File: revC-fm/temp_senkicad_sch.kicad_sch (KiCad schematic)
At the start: 4 parts, among them U32 MCP9700AT-E/LT

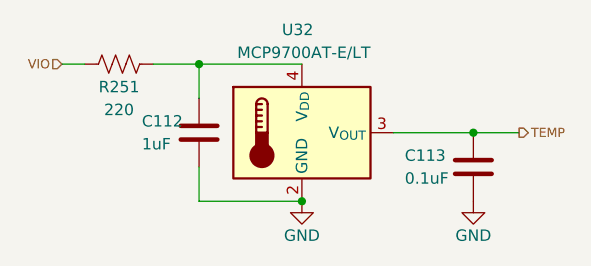
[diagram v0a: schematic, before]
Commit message: updated per review, improved docs
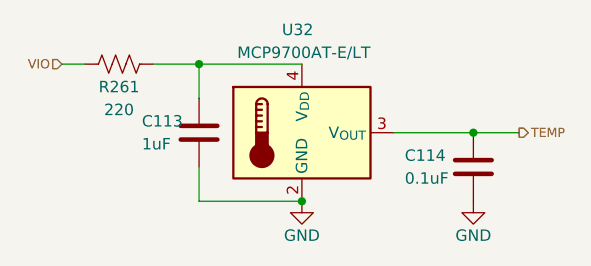
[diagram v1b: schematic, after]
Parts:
- renumbered C112 to C113, C113 to C114, R251 to R261
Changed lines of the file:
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@@
   (symbol (lib_id "power:GND") (at 148.59 104.14 0) (unit 1)
     (in_bom yes) (on_board yes) (dnp no)
-    (property "Reference" "#PWR0175" (at 148.59 110.49 0)
+    (property "Reference" "#PWR0180" (at 148.59 110.49 0)
       (effects (font (size 1.27 1.27)) hide)
     )
@@
       (project "mainboard"
         (path "/d1441985-7b63-4bf8-a06d-c70da2e3b78b/cda1ad7d-3729-4e28-9f04-75ded2a9befd/8821f222-8792-4e4d-9d02-2f4e81ef493f"
-          (reference "#PWR0175") (unit 1)
-        )
-        (path "/d1441985-7b63-4bf8-a06d-c70da2e3b78b/cda1ad7d-3729-4e28-9f04-75ded2a9befd/795619f3-8bd8-4f29-a923-296e7ed8459e"
-          (reference "#PWR0177") (unit 1)
-        )
-        (path "/d1441985-7b63-4bf8-a06d-c70da2e3b78b/cda1ad7d-3729-4e28-9f04-75ded2a9befd/e299339d-e625-4f2c-804c-bf3cf31a6799"
-          (reference "#PWR0179") (unit 1)
-        )
-        (path "/d1441985-7b63-4bf8-a06d-c70da2e3b78b/cda1ad7d-3729-4e28-9f04-75ded2a9befd/ea7f9fd6-aeb6-4ec9-906e-e84511ddb647"
-          (reference "#PWR0181") (unit 1)
+          (reference "#PWR0180") (unit 1)
+        )
+        (path "/d1441985-7b63-4bf8-a06d-c70da2e3b78b/cda1ad7d-3729-4e28-9f04-75ded2a9befd/795619f3-8bd8-4f29-a923-296e7ed8459e"
+          (reference "#PWR0182") (unit 1)
+        )
+        (path "/d1441985-7b63-4bf8-a06d-c70da2e3b78b/cda1ad7d-3729-4e28-9f04-75ded2a9befd/e299339d-e625-4f2c-804c-bf3cf31a6799"
+          (reference "#PWR0184") (unit 1)
+        )
+        (path "/d1441985-7b63-4bf8-a06d-c70da2e3b78b/cda1ad7d-3729-4e28-9f04-75ded2a9befd/ea7f9fd6-aeb6-4ec9-906e-e84511ddb647"
+          (reference "#PWR0186") (unit 1)
         )
       )
@@
   (symbol (lib_id "Device:R_US") (at 109.22 88.9 90) (unit 1)
     (in_bom yes) (on_board yes) (dnp no)
-    (property "Reference" "R251" (at 109.22 91.44 90)
+    (property "Reference" "R261" (at 109.22 91.44 90)
       (effects (font (size 1.27 1.27)))
     )
@@
       (effects (font (size 1.27 1.27)) hide)
     )
-    (pin "1")
-    (pin "2")
-    (instances
-      (project "mainboard"
-        (path "/d1441985-7b63-4bf8-a06d-c70da2e3b78b/cda1ad7d-3729-4e28-9f04-75ded2a9befd/8821f222-8792-4e4d-9d02-2f4e81ef493f"
-          (reference "R251") (unit 1)
-        )
-        (path "/d1441985-7b63-4bf8-a06d-c70da2e3b78b/cda1ad7d-3729-4e28-9f04-75ded2a9befd/795619f3-8bd8-4f29-a923-296e7ed8459e"
-          (reference "R252") (unit 1)
-        )
-        (path "/d1441985-7b63-4bf8-a06d-c70da2e3b78b/cda1ad7d-3729-4e28-9f04-75ded2a9befd/e299339d-e625-4f2c-804c-bf3cf31a6799"
-          (reference "R253") (unit 1)
-        )
-        (path "/d1441985-7b63-4bf8-a06d-c70da2e3b78b/cda1ad7d-3729-4e28-9f04-75ded2a9befd/ea7f9fd6-aeb6-4ec9-906e-e84511ddb647"
-          (reference "R254") (unit 1)
+    (property "Description" "RES 220 OHM 1% 1/10W 0603" (at 109.22 88.9 0)
+      (effects (font (size 1.27 1.27)) hide)
+    )
+    (pin "1")
+    (pin "2")
+    (instances
+      (project "mainboard"
+        (path "/d1441985-7b63-4bf8-a06d-c70da2e3b78b/cda1ad7d-3729-4e28-9f04-75ded2a9befd/8821f222-8792-4e4d-9d02-2f4e81ef493f"
+          (reference "R261") (unit 1)
+        )
+        (path "/d1441985-7b63-4bf8-a06d-c70da2e3b78b/cda1ad7d-3729-4e28-9f04-75ded2a9befd/795619f3-8bd8-4f29-a923-296e7ed8459e"
+          (reference "R262") (unit 1)
+        )
+        (path "/d1441985-7b63-4bf8-a06d-c70da2e3b78b/cda1ad7d-3729-4e28-9f04-75ded2a9befd/e299339d-e625-4f2c-804c-bf3cf31a6799"
+          (reference "R263") (unit 1)
+        )
+        (path "/d1441985-7b63-4bf8-a06d-c70da2e3b78b/cda1ad7d-3729-4e28-9f04-75ded2a9befd/ea7f9fd6-aeb6-4ec9-906e-e84511ddb647"
+          (reference "R264") (unit 1)
         )
       )
@@
     )
     (property "Manufacturer" "Microchip Technology" (at 129.54 96.52 0)
+      (effects (font (size 1.27 1.27)) hide)
+    )
+    (property "Description" "SENSOR ANALOG -40C-125C SC70-5" (at 129.54 96.52 0)
       (effects (font (size 1.27 1.27)) hide)
     )
@@
   (symbol (lib_id "power:GND") (at 129.54 104.14 0) (unit 1)
     (in_bom yes) (on_board yes) (dnp no)
-    (property "Reference" "#PWR0174" (at 129.54 110.49 0)
+    (property "Reference" "#PWR0179" (at 129.54 110.49 0)
       (effects (font (size 1.27 1.27)) hide)
     )
@@
       (project "mainboard"
         (path "/d1441985-7b63-4bf8-a06d-c70da2e3b78b/cda1ad7d-3729-4e28-9f04-75ded2a9befd/8821f222-8792-4e4d-9d02-2f4e81ef493f"
-          (reference "#PWR0174") (unit 1)
-        )
-        (path "/d1441985-7b63-4bf8-a06d-c70da2e3b78b/cda1ad7d-3729-4e28-9f04-75ded2a9befd/795619f3-8bd8-4f29-a923-296e7ed8459e"
-          (reference "#PWR0176") (unit 1)
-        )
-        (path "/d1441985-7b63-4bf8-a06d-c70da2e3b78b/cda1ad7d-3729-4e28-9f04-75ded2a9befd/e299339d-e625-4f2c-804c-bf3cf31a6799"
-          (reference "#PWR0178") (unit 1)
-        )
-        (path "/d1441985-7b63-4bf8-a06d-c70da2e3b78b/cda1ad7d-3729-4e28-9f04-75ded2a9befd/ea7f9fd6-aeb6-4ec9-906e-e84511ddb647"
-          (reference "#PWR0180") (unit 1)
+          (reference "#PWR0179") (unit 1)
+        )
+        (path "/d1441985-7b63-4bf8-a06d-c70da2e3b78b/cda1ad7d-3729-4e28-9f04-75ded2a9befd/795619f3-8bd8-4f29-a923-296e7ed8459e"
+          (reference "#PWR0181") (unit 1)
+        )
+        (path "/d1441985-7b63-4bf8-a06d-c70da2e3b78b/cda1ad7d-3729-4e28-9f04-75ded2a9befd/e299339d-e625-4f2c-804c-bf3cf31a6799"
+          (reference "#PWR0183") (unit 1)
+        )
+        (path "/d1441985-7b63-4bf8-a06d-c70da2e3b78b/cda1ad7d-3729-4e28-9f04-75ded2a9befd/ea7f9fd6-aeb6-4ec9-906e-e84511ddb647"
+          (reference "#PWR0185") (unit 1)
         )
       )
@@
   (symbol (lib_id "Device:C") (at 148.59 100.33 0) (unit 1)
     (in_bom yes) (on_board yes) (dnp no)
-    (property "Reference" "C113" (at 140.97 99.06 0)
+    (property "Reference" "C114" (at 140.97 99.06 0)
       (effects (font (size 1.27 1.27)) (justify left))
     )
@@
       (effects (font (size 1.27 1.27)) hide)
     )
+    (property "Description" "CAP CER 0.1UF 50V X7R 0402" (at 148.59 100.33 0)
+      (effects (font (size 1.27 1.27)) hide)
+    )
+    (pin "1")
+    (pin "2")
+    (instances
+      (project "mainboard"
+        (path "/d1441985-7b63-4bf8-a06d-c70da2e3b78b/cda1ad7d-3729-4e28-9f04-75ded2a9befd/8821f222-8792-4e4d-9d02-2f4e81ef493f"
+          (reference "C114") (unit 1)
+        )
+        (path "/d1441985-7b63-4bf8-a06d-c70da2e3b78b/cda1ad7d-3729-4e28-9f04-75ded2a9befd/795619f3-8bd8-4f29-a923-296e7ed8459e"
+          (reference "C116") (unit 1)
+        )
+        (path "/d1441985-7b63-4bf8-a06d-c70da2e3b78b/cda1ad7d-3729-4e28-9f04-75ded2a9befd/e299339d-e625-4f2c-804c-bf3cf31a6799"
+          (reference "C118") (unit 1)
+        )
+        (path "/d1441985-7b63-4bf8-a06d-c70da2e3b78b/cda1ad7d-3729-4e28-9f04-75ded2a9befd/ea7f9fd6-aeb6-4ec9-906e-e84511ddb647"
+          (reference "C120") (unit 1)
+        )
+      )
+    )
+  )
+  (symbol (lib_id "Device:C") (at 118.11 96.52 0) (unit 1)
+    (in_bom yes) (on_board yes) (dnp no)
+    (property "Reference" "C113" (at 111.76 95.25 0)
+      (effects (font (size 1.27 1.27)) (justify left))
+    )
+    (property "Value" "1uF" (at 111.76 97.79 0)
+      (effects (font (size 1.27 1.27)) (justify left))
+    )
+    (property "Footprint" "Capacitor_SMD:C_0603_1608Metric" (at 119.0752 100.33 0)
+      (effects (font (size 1.27 1.27)) hide)
+    )
+    (property "Datasheet" "~" (at 118.11 96.52 0)
+      (effects (font (size 1.27 1.27)) hide)
+    )
+    (property "Mfr. Part No" "CGA3E1X7R1V105K080AE" (at 118.11 96.52 0)
+      (effects (font (size 1.27 1.27)) hide)
+    )
+    (property "Manufacturer" "TDK" (at 118.11 96.52 0)
+      (effects (font (size 1.27 1.27)) hide)
+    )
+    (property "Description" "CAP CER 1UF 35V X7R 0603" (at 118.11 96.52 0)
+      (effects (font (size 1.27 1.27)) hide)
+    )
     (pin "1")
     (pin "2")
@@
         )
       )
-    )
-  )
-  (symbol (lib_id "Device:C") (at 118.11 96.52 0) (unit 1)
-    (in_bom yes) (on_board yes) (dnp no)
-    (property "Reference" "C112" (at 111.76 95.25 0)
-      (effects (font (size 1.27 1.27)) (justify left))
-    )
-    (property "Value" "1uF" (at 111.76 97.79 0)
-      (effects (font (size 1.27 1.27)) (justify left))
-    )
-    (property "Footprint" "Capacitor_SMD:C_0603_1608Metric" (at 119.0752 100.33 0)
-      (effects (font (size 1.27 1.27)) hide)
-    )
-    (property "Datasheet" "~" (at 118.11 96.52 0)
-      (effects (font (size 1.27 1.27)) hide)
-    )
-    (property "Mfr. Part No" "CGA3E1X7R1V105K080AE" (at 118.11 96.52 0)
-      (effects (font (size 1.27 1.27)) hide)
-    )
-    (property "Manufacturer" "TDK" (at 118.11 96.52 0)
-      (effects (font (size 1.27 1.27)) hide)
-    )
-    (pin "1")
-    (pin "2")
-    (instances
-      (project "mainboard"
-        (path "/d1441985-7b63-4bf8-a06d-c70da2e3b78b/cda1ad7d-3729-4e28-9f04-75ded2a9befd/8821f222-8792-4e4d-9d02-2f4e81ef493f"
-          (reference "C112") (unit 1)
-        )
-        (path "/d1441985-7b63-4bf8-a06d-c70da2e3b78b/cda1ad7d-3729-4e28-9f04-75ded2a9befd/795619f3-8bd8-4f29-a923-296e7ed8459e"
-          (reference "C114") (unit 1)
-        )
-        (path "/d1441985-7b63-4bf8-a06d-c70da2e3b78b/cda1ad7d-3729-4e28-9f04-75ded2a9befd/e299339d-e625-4f2c-804c-bf3cf31a6799"
-          (reference "C116") (unit 1)
-        )
-        (path "/d1441985-7b63-4bf8-a06d-c70da2e3b78b/cda1ad7d-3729-4e28-9f04-75ded2a9befd/ea7f9fd6-aeb6-4ec9-906e-e84511ddb647"
-          (reference "C118") (unit 1)
-        )
-      )
